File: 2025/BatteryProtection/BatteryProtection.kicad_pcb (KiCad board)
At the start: 4 copper layers, 90.9 x 36.6 mm, 43 parts, among them Q1 IXTA140P05T, Q10 BC849, Q11 BC849, Q2 BC849, Q3 BC849, Q4 BC849, Q5 BC849, Q6 BC849, Q7 BC849, Q8 BC849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

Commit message: started PCB layout
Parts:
- removed C5: 0.1uF, Capacitor_SMD:C_0603_1608Metric_Pad1.08x0.95mm_HandSolder
- removed D1: 4.7V, Diode_SMD:D_0603_1608Metric_Pad1.05x0.95mm_HandSolder
- removed D2: 5.6V, Diode_SMD:D_0603_1608Metric_Pad1.05x0.95mm_HandSolder
- added J1: Conn_01x02_Socket, Connector_JST:JST_XH_B2B-XH-A_1x02_P2.50mm_Vertical, F.Cu at (213.4, 116.0)
- added J2: Conn_01x02_Pin, BatteryProtection:XT90PW-M, F.Cu at (174.5, 46.0)
- added J3: Conn_01x02_Pin, BatteryProtection:XT90PW-F, F.Cu at (163.2, 153.7)
- added Q12: BC847, Package_TO_SOT_SMD:SOT-23, F.Cu at (157.1, 113.0)
- added R24: 10k, Resistor_SMD:R_0603_1608Metric_Pad0.98x0.95mm_HandSolder, F.Cu at (130.0, 109.5)
- added R25: 100k, Resistor_SMD:R_0603_1608Metric_Pad0.98x0.95mm_HandSolder, F.Cu at (146.0, 106.9)
- added U3: MCP1799x-330xxTT, Package_TO_SOT_SMD:SOT-23, F.Cu at (137.5, 113.5)
- C1, C2: value 10nF -> 1uF
- C3, C4: value 1uF -> 1u
- Q10, Q11, Q2, Q3, Q4, Q5, Q6, Q7, Q8, Q9: value BC849 -> BC847
- R1, R10: value 100k -> 50k
- R11: value Load -> 100k
- R14, R8: value 100k -> 1k
- R2: value 50k -> 10k
- R23: value 1k -> 10k
- R3: value 10k -> 116k
- R4: value 10k -> 15k
- R9: value 1k -> 100k
- U1, U2: value PLACEHOLDER -> MCP6561-OT
- moved R20 71.1 mm to (170.5, 137.9), turned to 90 degrees
- moved R19 71.0 mm to (164.2, 134.6), turned to 0 degrees
- moved R22 70.2 mm to (172.5, 127.0), turned to -90 degrees
- moved R15 69.1 mm to (167.5, 137.9), turned to 90 degrees
- moved R11 67.4 mm to (159.5, 138.0), turned to 90 degrees
- moved R18 66.8 mm to (166.7, 127.5), turned to 0 degrees
- moved R10 61.6 mm to (169.5, 120.6), turned to 90 degrees
- moved R17 59.5 mm to (157.4, 130.0)
- moved R21 59.0 mm to (161.5, 126.5), turned to -90 degrees
- moved R16 50.9 mm to (148.5, 129.4), turned to 90 degrees
- moved R14 47.0 mm to (153.6, 121.5)
- moved R12 45.2 mm to (155.5, 118.1), turned to 90 degrees
- moved R9 44.6 mm to (158.0, 108.6), turned to 90 degrees
- moved R13 43.8 mm to (153.0, 118.1), turned to 90 degrees
- moved Q5 42.3 mm to (164.0, 138.1)
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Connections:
- C1 pad 1: Net-(D2-K) -> GND
- C1 pad 2: GND -> +5V
- C2 pad 1: Net-(D1-K) -> GND
- C2 pad 2: GND -> +5V
- C3 pad 1: GND -> Vs
- C3 pad 2: Vs -> GND
- C4 pad 1: GND -> +5V
- C4 pad 2: Vs -> GND
- Q1 pad 3: Net-(Q1-S) -> VOUT
- Q2 pad 2: Net-(Q2-E) -> GND
- Q2 pad 3: Vs -> Net-(Q2-C)
- Q3 pad 2: Net-(Q2-E) -> GND
- Q3 pad 3: Vs -> Net-(Q2-C)
- Q4 pad 2: Net-(Q2-E) -> GND
- Q4 pad 3: Vs -> Net-(Q2-C)
- R1 pad 2: Net-(U1-+) -> Net-(U2--)
- R10 pad 1: Net-(Q1-G) -> GND
- R10 pad 2: Vs -> VOUT
- R11 pad 1: GND -> Net-(Q5-C)
- R11 pad 2: Net-(Q1-S) -> Vs
- R12 pad 1: Net-(Q5-C) -> Net-(Q6-C)
- R13 pad 1: Net-(Q6-C) -> Net-(Q8-C)
- R14 pad 1: Net-(Q8-C) -> Net-(Q6-C)
- R14 pad 2: Vs -> Net-(Q8-B)
- R15 pad 1: Net-(Q6-C) -> GPIO
- R15 pad 2: Net-(Q8-B) -> Net-(Q5-B)
- R16 pad 1: Net-(Q9-C) -> Net-(Q5-C)
- R16 pad 2: Net-(Q7-B) -> Net-(Q6-B)
- R17 pad 1: Net-(Q5-C) -> Net-(Q9-C)
- R17 pad 2: Net-(Q6-B) -> Net-(Q7-B)
- R18 pad 1: Gpio -> Net-(Q9-C)
- R18 pad 2: Net-(Q5-B) -> Net-(Q10-B)
- R19 pad 1: Net-(Q9-C) -> Net-(Q9-B)
- R19 pad 2: Net-(Q10-B) -> Net-(Q10-C)
- R2 pad 1: Net-(U1-+) -> Net-(U2--)
- R20 pad 1: Net-(Q9-B) -> GPIO
- R20 pad 2: Net-(Q10-C) -> Net-(Q11-B)
- R21 pad 1: Gpio -> Vs
- R21 pad 2: Net-(Q11-B) -> Net-(Q9-C)
- R22 pad 2: Net-(Q9-C) -> Net-(Q10-C)
- R23 pad 1: Vs -> Net-(U1--)
- R23 pad 2: Net-(Q10-C) -> GND
- R3 pad 2: Net-(D2-K) -> Net-(U1-+)
- R4 pad 1: Vs -> +5V
- R4 pad 2: Net-(D1-K) -> Net-(U1--)
- R8 pad 1: GND -> Net-(Q12-B)
- R8 pad 2: Net-(Q2-E) -> Net-(Q2-C)
- R9 pad 2: Net-(Q2-E) -> Vs
- U1 pad 1: Net-(D2-K) -> Net-(R5-Pad2)
- U1 pad 4: Net-(R5-Pad2) -> Net-(U1--)
- U1 pad 5: Vs -> +5V
- U2 pad 1: Net-(U1-+) -> Net-(R6-Pad1)
- U2 pad 3: Net-(D1-K) -> Net-(U1--)
- U2 pad 4: Net-(R6-Pad1) -> Net-(U2--)
- U2 pad 5: Vs -> +5V
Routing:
- net GND: track 0.00 -> 363.8 mm
- net Vs: track 0.00 -> 123.0 mm
- net Net-(Q9-C): track 0.00 -> 26.1 mm
- net +5V: track 0.00 -> 25.7 mm
- net Net-(Q5-C): track 0.00 -> 19.2 mm
- net Net-(Q2-C): track 0.00 -> 17.2 mm
- net Net-(Q6-C): track 0.00 -> 14.9 mm
- net GPIO: track 0.00 -> 12.6 mm
- net Net-(Q10-C): track 0.00 -> 12.1 mm
- net Net-(U1-+): track 0.00 -> 11.1 mm
- net Net-(Q1-G): track 0.00 -> 10.9 mm
- net Net-(U2--): track 0.00 -> 10.8 mm
- net Net-(Q4-B): track 0.00 -> 8.39 mm
- net Net-(Q8-C): track 0.00 -> 7.73 mm
- net Net-(Q11-B): track 0.00 -> 7.49 mm
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- added copper zone on F.Cu, net VOUT
- added copper zone on F.Cu, net Vs
- removed copper zone on B.Cu, net GND
- removed copper zone on F.Cu, net GND
- removed copper zone on In1.Cu, net GND
- removed copper zone on In2.Cu, net GND
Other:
- board size 90.9 x 36.6 mm -> 95.4 x 138.1 mm
- copper layers 4 -> 2
- board text added: "BATTERY INPUT"
- board text added: "GPIO"

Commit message: redrew PCB
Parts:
- moved J2 109.7 mm to (165.5, 155.2), turned to 0 degrees
- moved R5 85.3 mm to (220.6, 75.0)
- moved C4 85.3 mm to (220.0, 80.9)
- moved J1 82.2 mm to (172.0, 45.0), turned to 90 degrees
- moved R23 73.8 mm to (203.5, 92.5)
- moved R4 72.6 mm to (203.5, 87.6)
- moved C2 67.4 mm to (198.0, 82.5), turned to 0 degrees
- moved C3 66.4 mm to (197.6, 94.0), turned to 0 degrees
- moved U3 64.7 mm to (197.9, 90.5), turned to 180 degrees
- moved U1 64.6 mm to (197.9, 85.5), turned to 0 degrees
- moved U2 63.8 mm to (197.9, 98.0), turned to 180 degrees
- moved Q10 63.7 mm to (234.9, 123.9)
- moved Q11 63.7 mm to (229.9, 123.9)
- moved Q5 63.7 mm to (227.3, 130.9)
- moved Q6 63.7 mm to (212.3, 117.8)
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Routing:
- net GND: track 363.8 -> 32.6 mm
- net Vs: track 123.0 -> 54.4 mm
- net Net-(Q9-C): track 26.1 -> 0.00 mm
- net Net-(Q5-C): track 19.2 -> 0.00 mm
- net Net-(Q6-C): track 14.9 -> 0.00 mm
- net Net-(U1--): track 2.56 -> 15.7 mm
- net GPIO: track 12.6 -> 0.00 mm
- net Net-(Q10-C): track 12.1 -> 0.00 mm
- net Net-(Q4-B): track 8.39 -> 0.00 mm
- net Net-(Q2-C): track 17.2 -> 9.05 mm
- net Net-(Q8-C): track 7.73 -> 0.00 mm
- net Net-(Q11-B): track 7.49 -> 0.00 mm
- net Net-(Q2-B): track 6.47 -> 0.00 mm
- net Net-(R6-Pad1): track 6.31 -> 0.00 mm
- net Net-(Q3-B): track 5.64 -> 0.00 mm
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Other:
- board size 95.4 x 138.1 mm -> 65.4 x 137.1 mm

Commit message: different design on PCB uploaded
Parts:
- moved R10 87.3 mm to (182.5, 42.1), turned to -90 degrees
- moved R15 43.8 mm to (188.8, 118.8), turned to 0 degrees
- moved R20 43.3 mm to (192.1, 119.4)
- moved Q5 41.8 mm to (188.6, 115.2), turned to 180 degrees
- moved R11 39.3 mm to (188.7, 111.4), turned to 0 degrees
- moved Q10 39.2 mm to (195.7, 122.8), turned to -90 degrees
- moved R19 37.4 mm to (192.1, 115.5), turned to -90 degrees
- moved R22 36.4 mm to (199.7, 123.8), turned to 180 degrees
- moved Q11 34.7 mm to (195.7, 117.8), turned to 0 degrees
- moved Q9 31.4 mm to (195.6, 112.9), turned to 0 degrees
- moved R18 31.0 mm to (199.1, 118.0), turned to -90 degrees
- moved R5 30.9 mm to (190.6, 82.5), turned to 0 degrees
- moved R17 28.0 mm to (196.7, 108.7), turned to 90 degrees
- moved R16 27.1 mm to (188.6, 108.4), turned to 0 degrees
- moved R21 25.5 mm to (200.2, 112.9), turned to 180 degrees
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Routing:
- net Net-(Q10-C): track 0.00 -> 14.9 mm
- net Net-(Q9-C): track 0.00 -> 10.3 mm
- net Net-(Q5-C): track 0.00 -> 6.90 mm
- net Net-(Q6-E): track 0.00 -> 6.63 mm
- net GND: track 32.6 -> 38.5 mm
- net Net-(Q6-B): track 0.00 -> 4.96 mm
- net Net-(Q8-B): track 0.00 -> 4.43 mm
- net Net-(U1-+): track 14.1 -> 18.3 mm
- net Net-(Q10-B): track 0.00 -> 4.04 mm
- net Net-(Q9-B): track 0.00 -> 3.62 mm
- net Net-(Q11-B): track 0.00 -> 3.36 mm
- net Net-(Q7-B): track 0.00 -> 3.29 mm
- net Net-(Q5-B): track 0.00 -> 2.60 mm

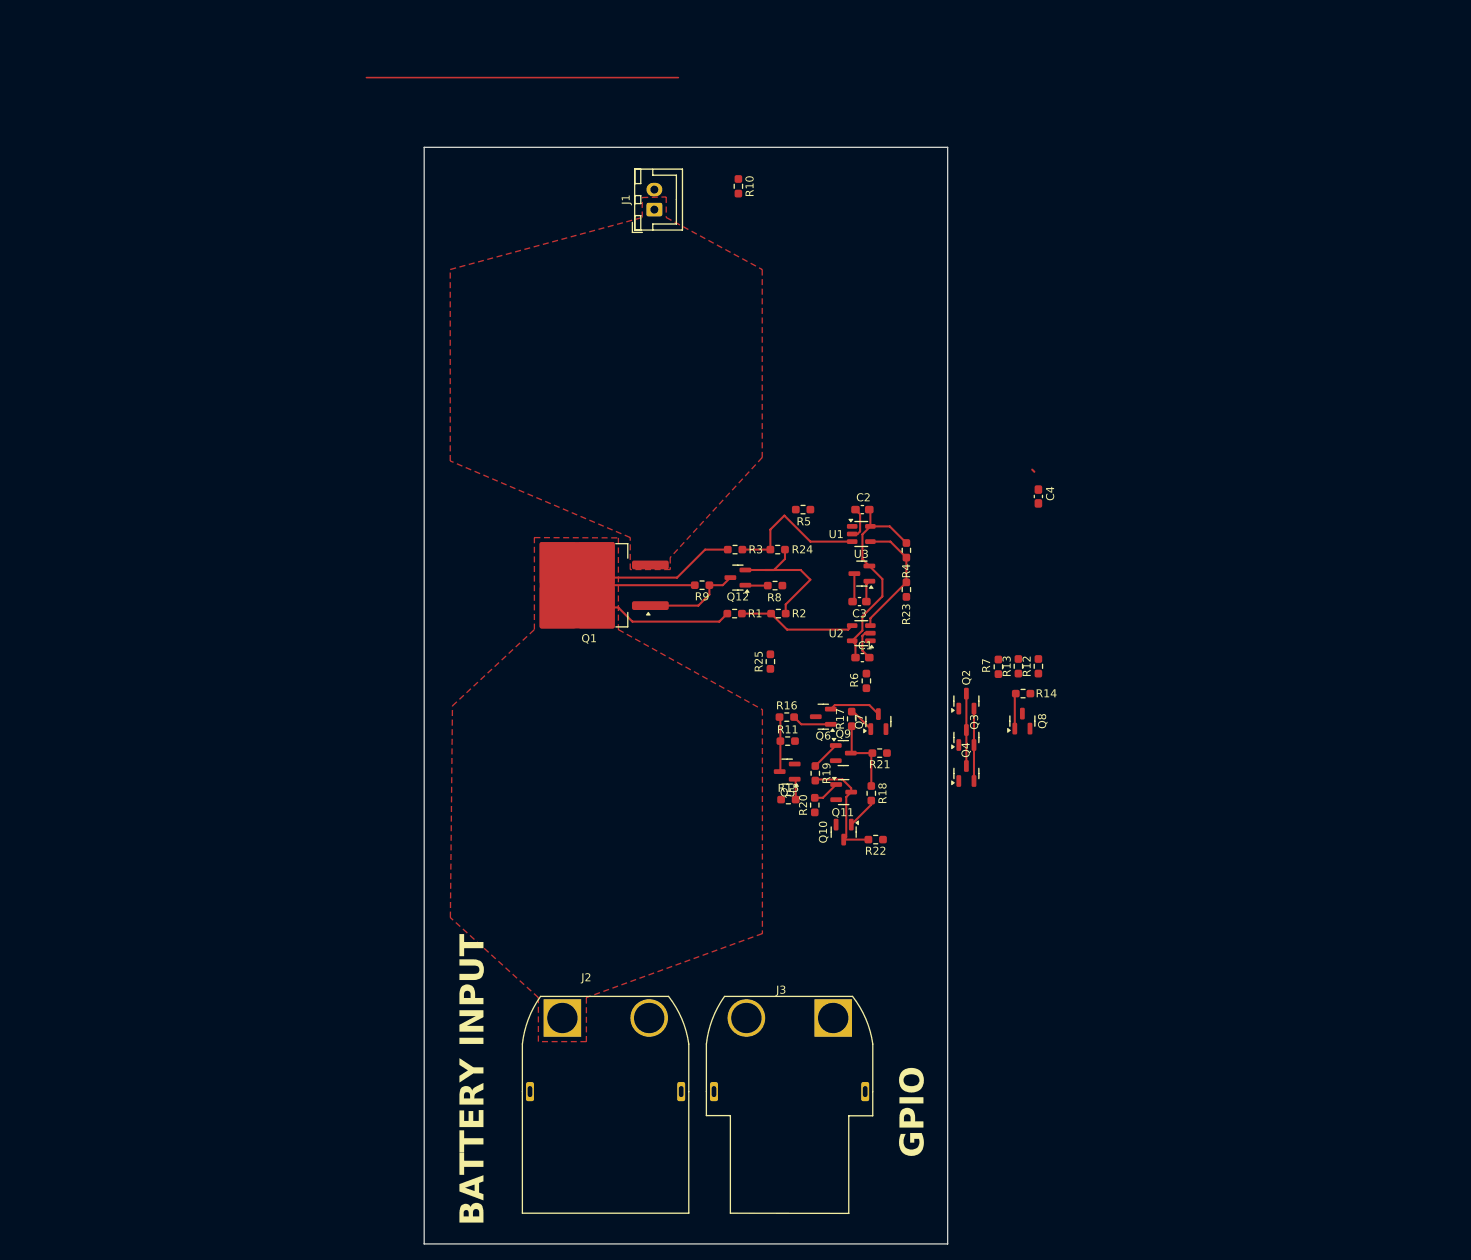
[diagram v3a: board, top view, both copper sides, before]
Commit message: missing one more wire
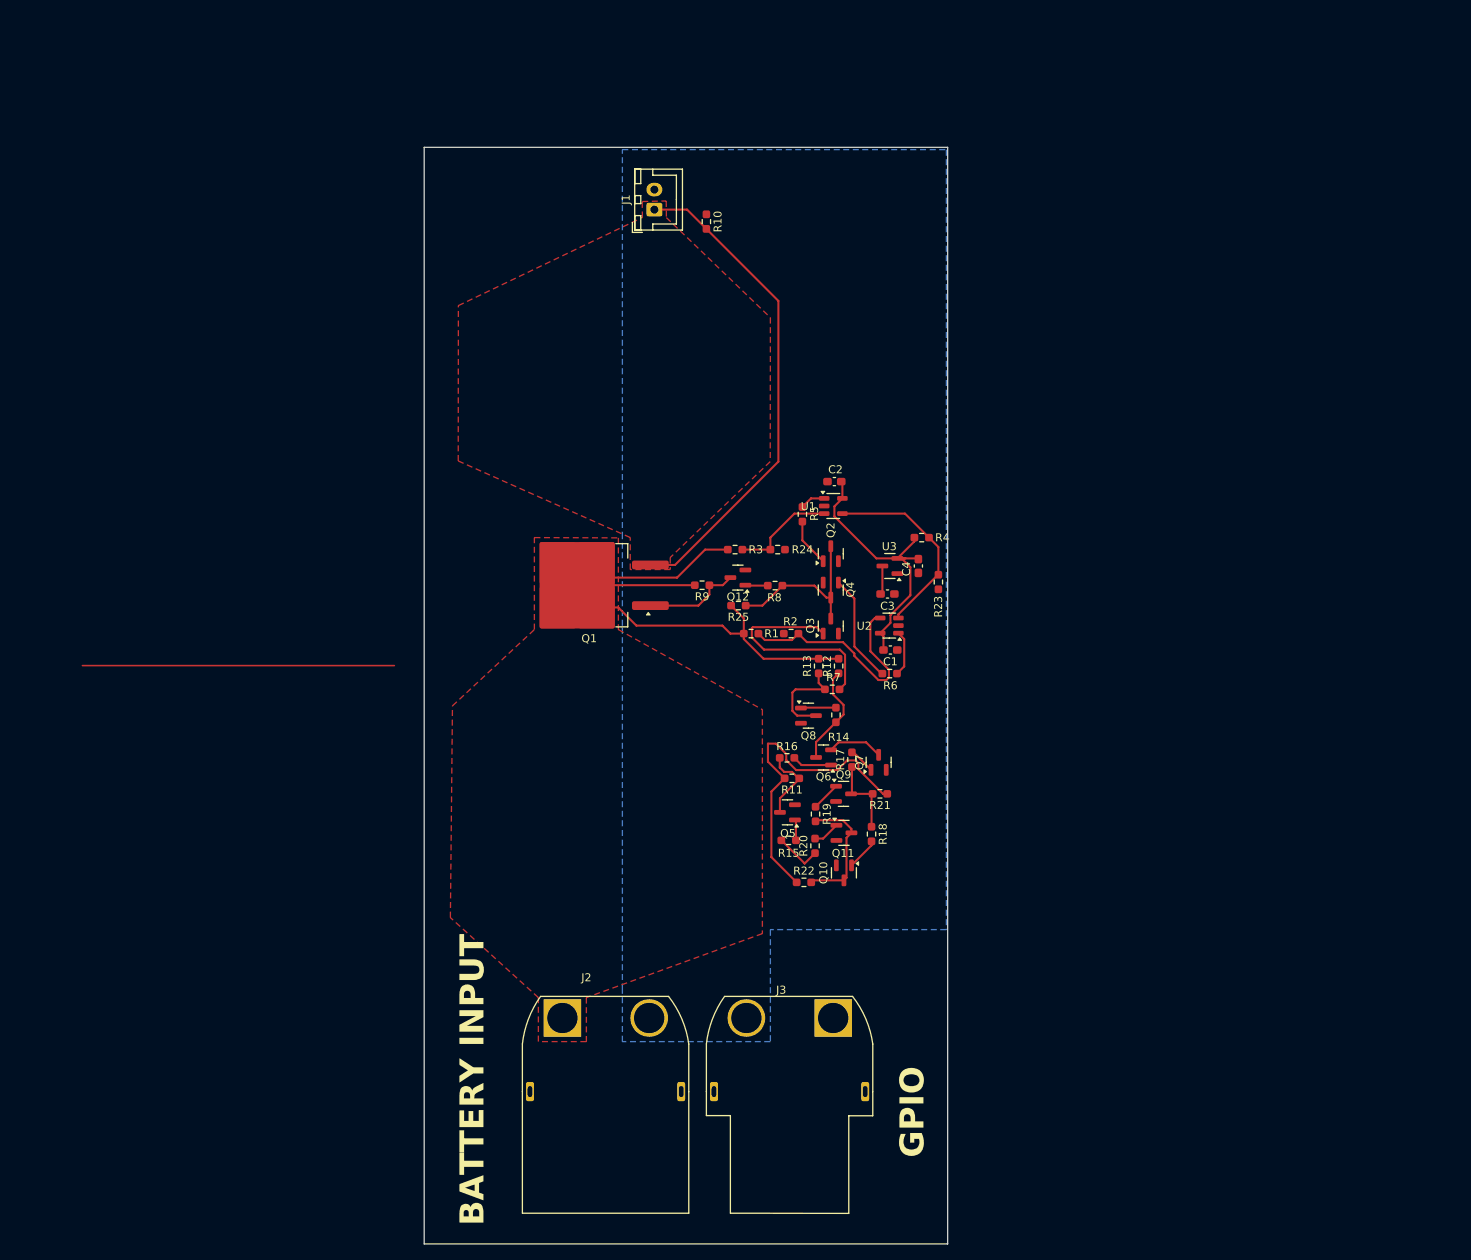
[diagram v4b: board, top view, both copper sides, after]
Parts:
- moved Q8 26.8 mm to (191.3, 108.3), turned to 0 degrees
- moved Q2 25.0 mm to (194.1, 88.0)
- moved Q3 25.0 mm to (194.1, 92.6), turned to -90 degrees
- moved Q4 25.0 mm to (194.1, 97.1)
- moved R12 25.0 mm to (195.0, 102.1)
- moved R13 25.0 mm to (192.5, 102.1)
- moved R14 23.5 mm to (194.7, 108.2), turned to 90 degrees
- moved R7 21.0 mm to (194.2, 105.0), turned to 0 degrees
- moved C4 17.3 mm to (205.0, 89.5), turned to -90 degrees
- moved R22 10.4 mm to (190.7, 129.1), turned to 0 degrees
- moved R25 8.06 mm to (182.5, 94.5), turned to 180 degrees
- moved R10 5.96 mm to (178.5, 46.5)
- moved Q10 5.09 mm to (195.7, 127.9)
- moved Q11 5.09 mm to (195.7, 122.9)
- moved Q5 5.09 mm to (188.6, 120.3)
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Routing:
- net VOUT: track 0.00 -> 61.7 mm
- net Vs: track 54.4 -> 114.0 mm
- net GND: track 38.5 -> 0.00 mm
- net Net-(Q4-B): track 0.00 -> 27.6 mm
- net Net-(U2--): track 14.8 -> 29.0 mm
- net Net-(Q3-B): track 0.00 -> 13.7 mm
- net Net-(Q6-C): track 0.00 -> 12.8 mm
- net Net-(Q2-C): track 9.05 -> 21.3 mm
- net Net-(Q8-C): track 0.00 -> 12.1 mm
- net Net-(U1--): track 15.7 -> 24.9 mm
- net +5V: track 27.5 -> 36.2 mm
- net Net-(Q2-B): track 0.00 -> 6.03 mm
- net GPIO: track 0.00 -> 5.95 mm
- net Net-(R6-Pad1): track 0.00 -> 5.73 mm
- net Net-(U1-+): track 18.3 -> 13.0 mm
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- added copper zone on B.Cu, net GND

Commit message: Made a complete PCB design
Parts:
- moved J3 123.2 mm to (161.5, 35.0), turned to -90 degrees
- moved J1 86.0 mm to (190.5, 129.0), turned to -90 degrees
- moved R10 11.5 mm to (177.5, 35.0)
- moved R12 9.55 mm to (185.5, 101.5)
- moved R13 9.55 mm to (183.0, 101.5)
- moved R7 9.55 mm to (184.7, 104.4)
- moved R23 7.01 mm to (200.5, 92.0), turned to 90 degrees
- moved R4 6.42 mm to (199.5, 83.5), turned to 180 degrees
- moved J2 5.48 mm to (161.5, 151.5), turned to -90 degrees
- moved R6 5.31 mm to (197.1, 100.0)
- moved C1 4.89 mm to (197.1, 98.0)
- moved C4 4.89 mm to (200.6, 87.5)
- moved U2 4.89 mm to (196.9, 95.0)
- moved U3 4.89 mm to (197.0, 87.5)
- moved Q10 4.67 mm to (195.7, 123.2)
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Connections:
- J1 pad 1: VOUT -> GPIO
- J3 pad 1: GPIO -> VOUT
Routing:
- net VOUT: track 61.7 -> 8.85 mm
- net Net-(Q4-B): track 27.6 -> 8.73 mm
- net Net-(U2--): track 29.0 -> 13.7 mm, vias 0 -> 2
- net GPIO: track 5.95 -> 15.8 mm
- net +5V: track 36.2 -> 26.6 mm, vias 0 -> 2
- net Net-(U1--): track 24.9 -> 16.4 mm, vias 0 -> 2
- net GND: track 0.00 -> 8.49 mm, vias 0 -> 21
- net Vs: track 114.0 -> 121.0 mm, vias 0 -> 5
- net Net-(Q3-B): track 13.7 -> 9.78 mm
- net Net-(Q6-C): track 12.8 -> 15.5 mm, vias 0 -> 2
- net Net-(Q2-C): track 21.3 -> 19.3 mm
- net Net-(Q5-C): track 9.40 -> 7.99 mm
- net Net-(R6-Pad1): track 5.73 -> 4.69 mm
- net Net-(Q2-B): track 6.03 -> 5.12 mm, vias 0 -> 2
- net Net-(Q10-C): track 16.0 -> 16.7 mm
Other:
- board size 65.4 x 137.1 mm -> 58.4 x 140.1 mm
- board text added: "BAT IN"
- board text added: "BAT OUT"
- board text removed: "BATTERY INPUT"

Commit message: more work on PCB
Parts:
- added D1: LED, LED_SMD:LED_0805_2012Metric, F.Cu at (209.3, 103.0)
- added R26: 2.2k, Resistor_SMD:R_0603_1608Metric_Pad0.98x0.95mm_HandSolder, F.Cu at (179.0, 101.5)
- added TP1: GPIO, TestPoint:TestPoint_Pad_D1.5mm, F.Cu at (208.8, 95.5)
- added TP2: Vout, TestPoint:TestPoint_Pad_D1.5mm, F.Cu at (208.8, 99.0)
- added TP3: Vin, TestPoint:TestPoint_Pad_D1.5mm, F.Cu at (212.4, 95.5)
- added TP4: U1 Out, TestPoint:TestPoint_Pad_D1.5mm, F.Cu at (212.4, 99.0)
- added TP5: U2 Out, TestPoint:TestPoint_Pad_D1.5mm, F.Cu at (215.9, 95.5)
- added TP6: Kill, TestPoint:TestPoint_Pad_D1.5mm, F.Cu at (215.9, 99.0)
- added TP7: Vout, TestPoint:TestPoint_Pad_D1.5mm, F.Cu at (219.5, 95.5)
- added TP8: Pmos In, TestPoint:TestPoint_Pad_D1.5mm, F.Cu at (219.5, 99.0)
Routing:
- net GND: track 8.49 -> 35.6 mm, vias 21 -> 19
- net Vs: track 121.0 -> 130.4 mm
- net Net-(U2--): track 13.7 -> 20.0 mm
- net +5V: track 26.6 -> 31.9 mm
- net Net-(U1--): track 16.4 -> 20.2 mm
- net Net-(Q2-B): track 5.12 -> 8.39 mm
- net Net-(Q5-C): track 7.99 -> 8.87 mm
- net Net-(Q7-B): track 3.29 -> 3.97 mm
- net Net-(Q9-B): track 3.62 -> 4.28 mm
- net Net-(Q10-B): track 4.04 -> 4.65 mm
- net Net-(Q6-E): track 6.99 -> 7.59 mm

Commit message: more edits
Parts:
- moved TP2 66.9 mm to (175.5, 41.0)
- moved TP3 57.9 mm to (154.5, 94.5)
- moved TP8 42.1 mm to (178.5, 89.5)
- moved TP1 36.3 mm to (195.0, 129.0)
- moved TP6 36.0 mm to (180.0, 99.5)
- moved TP7 32.8 mm to (201.0, 122.5)
- moved D1 30.8 mm to (178.5, 102.0)
- moved TP4 30.6 mm to (187.0, 82.0)
- moved TP5 16.6 mm to (200.5, 101.5)
- moved R26 3.60 mm to (176.5, 98.9), turned to -90 degrees
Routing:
- net Net-(D1-A): track 12.0 -> 18.5 mm, vias 0 -> 2
- net Net-(Q9-C): track 10.3 -> 16.1 mm
- net VOUT: track 8.85 -> 13.7 mm
- net GPIO: track 15.8 -> 20.3 mm
- net Net-(R6-Pad1): track 4.69 -> 8.46 mm
- net Net-(R5-Pad2): track 3.17 -> 6.74 mm
- net Net-(D1-K): track 0.00 -> 2.62 mm
- net Net-(Q1-G): track 12.1 -> 14.2 mm
- net GND: track 35.6 -> 37.1 mm, vias 19 -> 20

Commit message: DID the voltage protection PCB
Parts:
- moved J3 104.7 mm to (257.9, 75.8), turned to 180 degrees
- moved R10 98.4 mm to (257.9, 91.8), turned to 180 degrees
- moved TP2 90.6 mm to (251.9, 89.8), turned to -90 degrees
- moved J2 78.4 mm to (141.4, 75.8), turned to 180 degrees
- moved TP3 50.9 mm to (198.4, 68.8), turned to -90 degrees
- moved Q1 39.6 mm to (201.0, 78.1), turned to 90 degrees
- moved TP1 36.8 mm to (163.9, 109.3), turned to -90 degrees
- moved J1 36.0 mm to (163.9, 104.8), turned to 180 degrees
- moved C2 35.5 mm to (213.9, 108.8), turned to -90 degrees
- moved R4 31.8 mm to (209.4, 113.8), turned to 90 degrees
- moved TP7 31.4 mm to (170.4, 115.3), turned to -90 degrees
- moved U1 31.3 mm to (210.9, 108.6), turned to -90 degrees
- moved TP4 30.7 mm to (210.9, 101.3), turned to -90 degrees
- moved R22 29.5 mm to (168.5, 104.9), turned to -90 degrees
- moved Q10 29.2 mm to (169.7, 109.9), turned to 180 degrees
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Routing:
- net Vs: track 130.4 -> 136.9 mm
- net Net-(D1-A): track 18.5 -> 20.1 mm
- net GND: track 37.1 -> 37.6 mm, vias 20 -> 19
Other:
- board size 58.4 x 140.1 mm -> 140.1 x 58.4 mm
